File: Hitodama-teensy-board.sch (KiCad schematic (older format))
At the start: 5 parts, among them U4 Teensy3.6

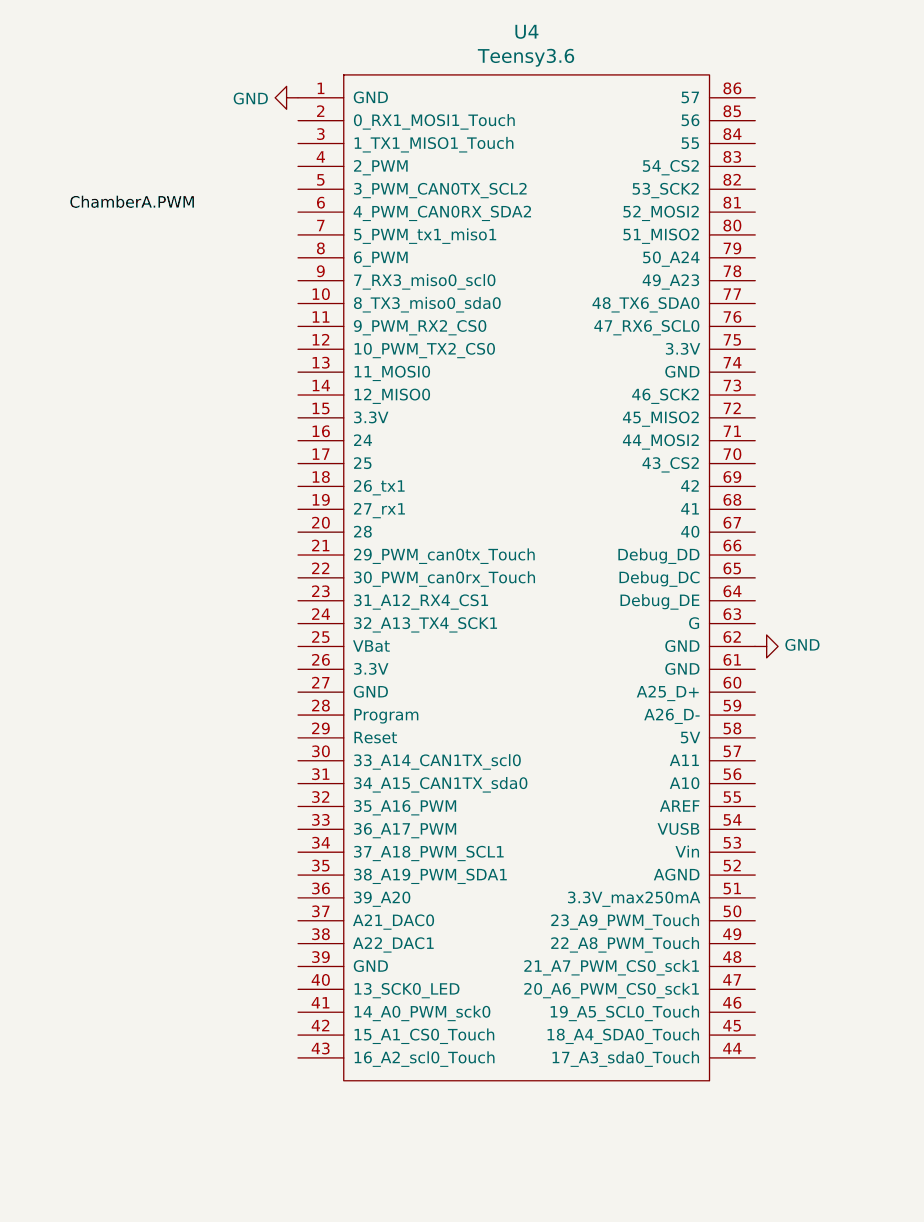
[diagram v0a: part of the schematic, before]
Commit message: Label all valve&motor controlle pins @ teensy
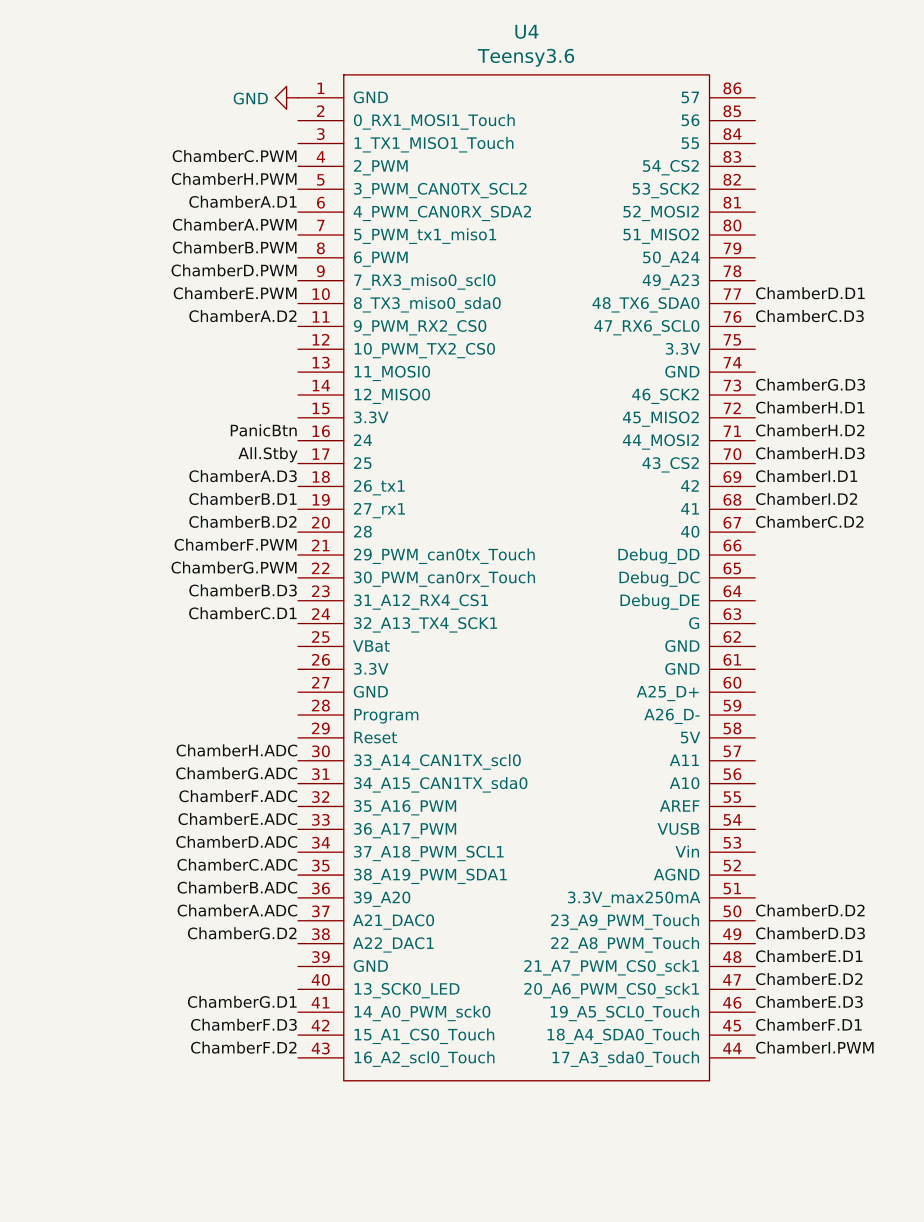
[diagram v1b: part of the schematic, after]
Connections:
- net ChamberA.PWM: now also U4.7 (5_PWM_tx1_miso1)
- net GND: no longer U4.62 (GND)
- net ChamberE.PWM: now reaches U4.10 (8_TX3_miso0_sda0)
- net ChamberA.D2: now reaches U4.11 (9_PWM_RX2_CS0)
- net PanicBtn: now reaches U4.16 (24)
- net All.Stby: now reaches U4.17 (25)
- net ChamberA.D3: now reaches U4.18 (26_tx1)
- net ChamberB.D1: now reaches U4.19 (27_rx1)
- net ChamberB.D2: now reaches U4.20 (28)
- net ChamberF.PWM: now reaches U4.21 (29_PWM_can0tx_Touch)
- net ChamberG.PWM: now reaches U4.22 (30_PWM_can0rx_Touch)
- net ChamberB.D3: now reaches U4.23 (31_A12_RX4_CS1)
- net ChamberC.D1: now reaches U4.24 (32_A13_TX4_SCK1)
- net ChamberH.ADC: now reaches U4.30 (33_A14_CAN1TX_scl0)
- net ChamberG.ADC: now reaches U4.31 (34_A15_CAN1TX_sda0)
- net ChamberF.ADC: now reaches U4.32 (35_A16_PWM)
- net ChamberE.ADC: now reaches U4.33 (36_A17_PWM)
- net ChamberD.ADC: now reaches U4.34 (37_A18_PWM_SCL1)
- net ChamberC.ADC: now reaches U4.35 (38_A19_PWM_SDA1)
- net ChamberB.ADC: now reaches U4.36 (39_A20)
- net ChamberA.ADC: now reaches U4.37 (A21_DAC0)
- net ChamberG.D2: now reaches U4.38 (A22_DAC1)
- net ChamberC.PWM: now reaches U4.4 (2_PWM)
- net ChamberG.D1: now reaches U4.41 (14_A0_PWM_sck0)
- net ChamberF.D3: now reaches U4.42 (15_A1_CS0_Touch)
- net ChamberF.D2: now reaches U4.43 (16_A2_scl0_Touch)
- net ChamberI.PWM: now reaches U4.44 (17_A3_sda0_Touch)
- net ChamberF.D1: now reaches U4.45 (18_A4_SDA0_Touch)
- net ChamberE.D3: now reaches U4.46 (19_A5_SCL0_Touch)
- net ChamberE.D2: now reaches U4.47 (20_A6_PWM_CS0_sck1)
- net ChamberE.D1: now reaches U4.48 (21_A7_PWM_CS0_sck1)
- net ChamberD.D3: now reaches U4.49 (22_A8_PWM_Touch)
- net ChamberH.PWM: now reaches U4.5 (3_PWM_CAN0TX_SCL2)
- net ChamberD.D2: now reaches U4.50 (23_A9_PWM_Touch)
- net ChamberA.D1: now reaches U4.6 (4_PWM_CAN0RX_SDA2)
- net ChamberC.D2: now reaches U4.67 (40)
- net ChamberI.D2: now reaches U4.68 (41)
- net ChamberI.D1: now reaches U4.69 (42)
- net ChamberH.D3: now reaches U4.70 (43_CS2)
- net ChamberH.D2: now reaches U4.71 (44_MOSI2)
- net ChamberH.D1: now reaches U4.72 (45_MISO2)
- net ChamberG.D3: now reaches U4.73 (46_SCK2)
- net ChamberC.D3: now reaches U4.76 (47_RX6_SCL0)
- net ChamberD.D1: now reaches U4.77 (48_TX6_SDA0)
- net ChamberB.PWM: now reaches U4.8 (6_PWM)
- net ChamberD.PWM: now reaches U4.9 (7_RX3_miso0_scl0)
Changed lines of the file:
@@
 EESchema Schematic File Version 4
+LIBS:Hitodama-teensy-board-cache
 EELAYER 26 0
 EELAYER END
@@
 	1    7150 1250
 	0    1    1    0
-$EndComp
-$Comp
-L power:GND #PWR0102
-U 1 1 5CB5BA86
-P 9150 3650
-F 0 "#PWR0102" H 9150 3400 50  0001 C CNN
-F 1 "GND" V 9155 3522 50  0000 R CNN
-F 2 "" H 9150 3650 50  0001 C CNN
-F 3 "" H 9150 3650 50  0001 C CNN
-	1    9150 3650
-	0    -1   -1   0
 $EndComp
 $Comp
@@
 	1    0    0    -1
 $EndComp
-Text Label 6150 1750 0    50   ~ 0
+Text Label 7150 1850 2    50   ~ 0
 ChamberA.PWM
+Text Label 7150 1950 2    50   ~ 0
+ChamberB.PWM
+Text Label 7150 1550 2    50   ~ 0
+ChamberC.PWM
+Text Label 7150 2050 2    50   ~ 0
+ChamberD.PWM
+Text Label 7150 2150 2    50   ~ 0
+ChamberE.PWM
+Text Label 7150 3250 2    50   ~ 0
+ChamberF.PWM
+Text Label 7150 3350 2    50   ~ 0
+ChamberG.PWM
+Text Label 7150 1650 2    50   ~ 0
+ChamberH.PWM
+Text Label 9150 5450 0    50   ~ 0
+ChamberI.PWM
+Text Label 7150 1750 2    50   ~ 0
+ChamberA.D1
+Text Label 7150 3050 2    50   ~ 0
+ChamberB.D1
+Text Label 7150 3550 2    50   ~ 0
+ChamberC.D1
+Text Label 9150 2150 0    50   ~ 0
+ChamberD.D1
+Text Label 9150 5050 0    50   ~ 0
+ChamberE.D1
+Text Label 9150 5350 0    50   ~ 0
+ChamberF.D1
+Text Label 7150 5250 2    50   ~ 0
+ChamberG.D1
+Text Label 9150 2650 0    50   ~ 0
+ChamberH.D1
+Text Label 9150 2950 0    50   ~ 0
+ChamberI.D1
+Text Label 7150 2250 2    50   ~ 0
+ChamberA.D2
+Text Label 7150 3150 2    50   ~ 0
+ChamberB.D2
+Text Label 9150 3150 0    50   ~ 0
+ChamberC.D2
+Text Label 9150 4850 0    50   ~ 0
+ChamberD.D2
+Text Label 9150 5150 0    50   ~ 0
+ChamberE.D2
+Text Label 7150 5450 2    50   ~ 0
+ChamberF.D2
+Text Label 7150 4950 2    50   ~ 0
+ChamberG.D2
+Text Label 9150 2750 0    50   ~ 0
+ChamberH.D2
+Text Label 9150 3050 0    50   ~ 0
+ChamberI.D2
+Text Label 7150 2950 2    50   ~ 0
+ChamberA.D3
+Text Label 7150 3450 2    50   ~ 0
+ChamberB.D3
+Text Label 9150 2250 0    50   ~ 0
+ChamberC.D3
+Text Label 9150 4950 0    50   ~ 0
+ChamberD.D3
+Text Label 9150 5250 0    50   ~ 0
+ChamberE.D3
+Text Label 7150 5350 2    50   ~ 0
+ChamberF.D3
+Text Label 9150 2550 0    50   ~ 0
+ChamberG.D3
+Text Label 9150 2850 0    50   ~ 0
+ChamberH.D3
+Text Label 7150 4850 2    50   ~ 0
+ChamberA.ADC
+Text Label 7150 4750 2    50   ~ 0
+ChamberB.ADC
+Text Label 7150 4650 2    50   ~ 0
+ChamberC.ADC
+Text Label 7150 4550 2    50   ~ 0
+ChamberD.ADC
+Text Label 7150 4450 2    50   ~ 0
+ChamberE.ADC
+Text Label 7150 4350 2    50   ~ 0
+ChamberF.ADC
+Text Label 7150 4250 2    50   ~ 0
+ChamberG.ADC
+Text Label 7150 4150 2    50   ~ 0
+ChamberH.ADC
+Text Label 7150 2750 2    50   ~ 0
+PanicBtn
+Text Label 7150 2850 2    50   ~ 0
+All.Stby
 $EndSCHEMATC

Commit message: Coordinate Connectors on both boards
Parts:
- added ChamberA1, ChamberB1, ChamberC1, ChamberD1, ChamberE1, ChamberF1, ChamberG1, ChamberH1, ChamberI1: ChamberBoard_Holder, chamber_board_holder:chamber_board_holder, symbol Hitodama~custom~parts:ChamberBoard_Holder
- added H5, H6: MountingHole, MountingHole:MountingHole_3.2mm_M3, symbol Mechanical:MountingHole
- added J1: Conn_01x12_Male, Connector_PinHeader_1.27mm:PinHeader_1x12_P1.27mm_Vertical, symbol Connector:Conn_01x12_Male
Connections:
- net labels added: +12V, +3.3V, A10, A11, A24, ChamberI.ADC, ChamberI.D3, D51, D52, D53, D54, D56, D57, SPI0.CS0, SPI0.MISO, SPI0.MOSI, SPI0.SCK, VCC
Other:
- moved on the sheet: H1, H2, H3, H4, U4

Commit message: schematic add SPI ports & 12 v power connector
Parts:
- removed J1: Conn_01x12_Male, Connector_PinHeader_1.27mm:PinHeader_1x12_P1.27mm_Vertical, symbol Connector:Conn_01x12_Male
- added J1: Jack-DC, Connector_BarrelJack:BarrelJack_Horizontal, symbol Connector:Jack-DC
- added SPIO_0, SPIO_1, SPIO_2, SPIO_3, SPIO_4: Conn_01x06_Female, Connector_PinHeader_2.54mm:PinHeader_1x06_P2.54mm_Vertical, symbol Connector:Conn_01x06_Female
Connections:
- net labels added: SPI0.CS1, SPI0.CS2, SPI0.CS3, SPI0.CS4
- net labels removed: D51, D52, D53, D54

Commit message: separated the teensy board into four modules, so that it fits in smaller PCB's. Improved the chamber board, and added rules so that auto-router can figure out the optimal 1 layer+jumpers route
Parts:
- removed ChamberA1, ChamberB1, ChamberC1, ChamberD1, ChamberE1, ChamberF1, ChamberG1, ChamberH1, ChamberI1: ChamberBoard_Holder, chamber_board_holder:chamber_board_holder, symbol Hitodama~custom~parts:ChamberBoard_Holder
- added J2, J3, J4: Conn_01x21_Female, Connector_PinHeader_2.54mm:PinHeader_1x21_P2.54mm_Vertical, symbol Connector:Conn_01x21_Female
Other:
- moved on the sheet: H1, H2, H3, H4, H5, H6, J1, SPIO_0, SPIO_1, SPIO_2, SPIO_3, SPIO_4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

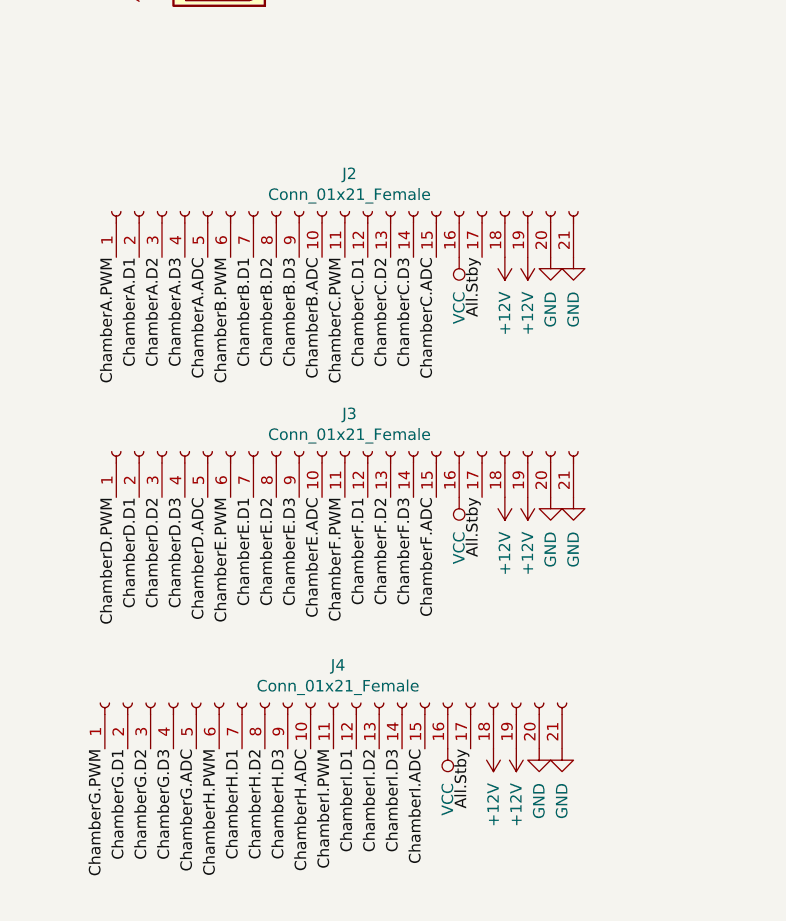
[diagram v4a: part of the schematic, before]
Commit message: teensy board change 21 pins headers into 20 pins headers.
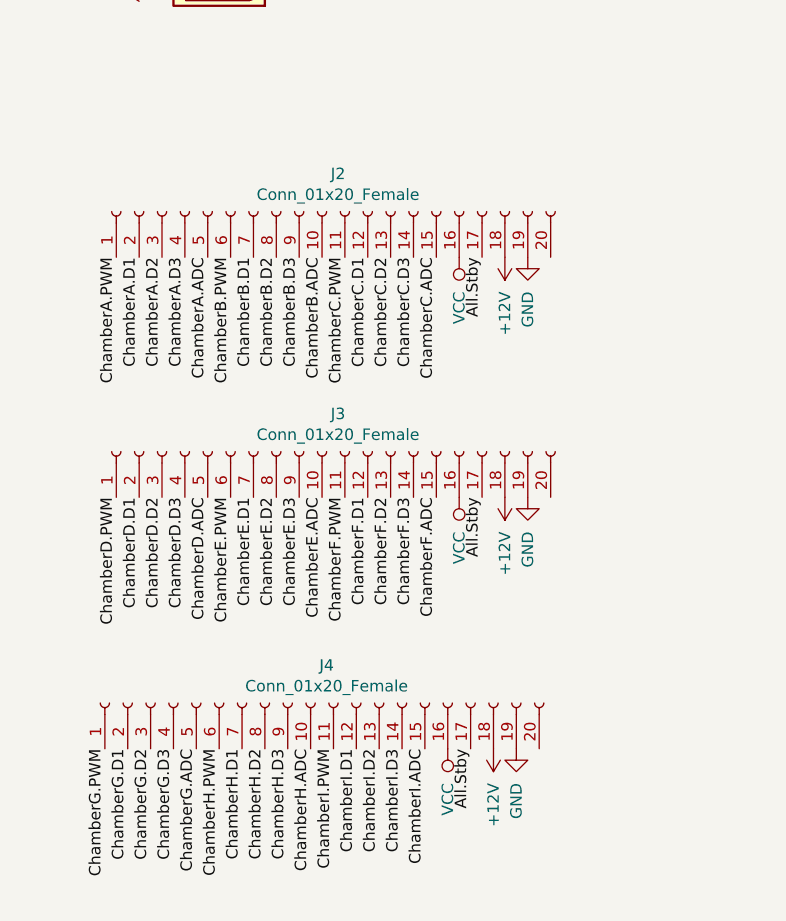
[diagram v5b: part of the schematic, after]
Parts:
- removed J2, J3, J4: Conn_01x21_Female, Connector_PinHeader_2.54mm:PinHeader_1x21_P2.54mm_Vertical, symbol Connector:Conn_01x21_Female
- added J2, J3, J4: Conn_01x20_Female, Connector_PinHeader_2.54mm:PinHeader_1x20_P2.54mm_Vertical, symbol Connector:Conn_01x20_Female
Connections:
- net +12V: now also J2.18 (Pin_18), J3.18 (Pin_18), J4.18 (Pin_18)
- net All.Stby: now also J2.17 (Pin_17), J3.17 (Pin_17), J4.17 (Pin_17)
- net ChamberA.ADC: now also J2.5 (Pin_5)
- net ChamberA.D1: now also J2.2 (Pin_2)
- net ChamberA.D2: now also J2.3 (Pin_3)
- net ChamberA.D3: now also J2.4 (Pin_4)
- net ChamberA.PWM: now also J2.1 (Pin_1)
- net ChamberB.ADC: now also J2.10 (Pin_10)
- net ChamberB.D1: now also J2.7 (Pin_7)
- net ChamberB.D2: now also J2.8 (Pin_8)
- net ChamberB.D3: now also J2.9 (Pin_9)
- net ChamberB.PWM: now also J2.6 (Pin_6)
- net ChamberC.ADC: now also J2.15 (Pin_15)
- net ChamberC.D1: now also J2.12 (Pin_12)
- net ChamberC.D2: now also J2.13 (Pin_13)
- net ChamberC.D3: now also J2.14 (Pin_14)
- net ChamberC.PWM: now also J2.11 (Pin_11)
- net ChamberD.ADC: now also J3.5 (Pin_5)
- net ChamberD.D1: now also J3.2 (Pin_2)
- net ChamberD.D2: now also J3.3 (Pin_3)
- net ChamberD.D3: now also J3.4 (Pin_4)
- net ChamberD.PWM: now also J3.1 (Pin_1)
- net ChamberE.ADC: now also J3.10 (Pin_10)
- net ChamberE.D1: now also J3.7 (Pin_7)
- net ChamberE.D2: now also J3.8 (Pin_8)
- net ChamberE.D3: now also J3.9 (Pin_9)
- net ChamberE.PWM: now also J3.6 (Pin_6)
- net ChamberF.ADC: now also J3.15 (Pin_15)
- net ChamberF.D1: now also J3.12 (Pin_12)
- net ChamberF.D2: now also J3.13 (Pin_13)
- net ChamberF.D3: now also J3.14 (Pin_14)
- net ChamberF.PWM: now also J3.11 (Pin_11)
- net ChamberG.ADC: now also J4.5 (Pin_5)
- net ChamberG.D1: now also J4.2 (Pin_2)
- net ChamberG.D2: now also J4.3 (Pin_3)
- net ChamberG.D3: now also J4.4 (Pin_4)
- net ChamberG.PWM: now also J4.1 (Pin_1)
- net ChamberH.ADC: now also J4.10 (Pin_10)
- net ChamberH.D1: now also J4.7 (Pin_7)
- net ChamberH.D2: now also J4.8 (Pin_8)
- net ChamberH.D3: now also J4.9 (Pin_9)
- net ChamberH.PWM: now also J4.6 (Pin_6)
- net ChamberI.ADC: now also J4.15 (Pin_15)
- net ChamberI.D1: now also J4.12 (Pin_12)
- net ChamberI.D2: now also J4.13 (Pin_13)
- net ChamberI.D3: now also J4.14 (Pin_14)
- net ChamberI.PWM: now also J4.11 (Pin_11)
- net GND: now also J2.19 (Pin_19), J3.19 (Pin_19), J4.19 (Pin_19)
- net VCC: now also J2.16 (Pin_16), J3.16 (Pin_16), J4.16 (Pin_16)
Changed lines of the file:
@@
 	-1   0    0    1
-$EndComp
-$Comp
-L Connector:Conn_01x21_Female J2
-U 1 1 5CC810CC
-P 2200 4550
-F 0 "J2" V 2365 4530 50  0000 C CNN
-F 1 "Conn_01x21_Female" V 2274 4530 50  0000 C CNN
-F 2 "Connector_PinHeader_2.54mm:PinHeader_1x21_P2.54mm_Vertical" H 2200 4550 50  0001 C CNN
-F 3 "~" H 2200 4550 50  0001 C CNN
-	1    2200 4550
-	0    -1   -1   0
 $EndComp
 Text Label 1200 4750 3    50   ~ 0
@@
 $EndComp
 $Comp
-L power:+12V #PWR0105
-U 1 1 5CC82883
+L power:GND #PWR0106
+U 1 1 5CC8290B
 P 3000 4750
-F 0 "#PWR0105" H 3000 4600 50  0001 C CNN
-F 1 "+12V" V 3000 4900 50  0000 L CNN
+F 0 "#PWR0106" H 3000 4500 50  0001 C CNN
+F 1 "GND" V 3000 4600 50  0000 R CNN
 F 2 "" H 3000 4750 50  0001 C CNN
 F 3 "" H 3000 4750 50  0001 C CNN
 	1    3000 4750
-	-1   0    0    1
-$EndComp
-$Comp
-L power:GND #PWR0106
-U 1 1 5CC8290B
-P 3100 4750
-F 0 "#PWR0106" H 3100 4500 50  0001 C CNN
-F 1 "GND" V 3100 4600 50  0000 R CNN
-F 2 "" H 3100 4750 50  0001 C CNN
-F 3 "" H 3100 4750 50  0001 C CNN
-	1    3100 4750
-	1    0    0    -1
-$EndComp
-$Comp
-L power:GND #PWR0107
-U 1 1 5CC829E5
-P 3200 4750
-F 0 "#PWR0107" H 3200 4500 50  0001 C CNN
-F 1 "GND" V 3200 4600 50  0000 R CNN
-F 2 "" H 3200 4750 50  0001 C CNN
-F 3 "" H 3200 4750 50  0001 C CNN
-	1    3200 4750
 	1    0    0    -1
 $EndComp
@@
 	1    2700 4750
 	-1   0    0    1
-$EndComp
-$Comp
-L Connector:Conn_01x21_Female J3
-U 1 1 5CC80D90
-P 2200 5600
-F 0 "J3" V 2365 5580 50  0000 C CNN
-F 1 "Conn_01x21_Female" V 2274 5580 50  0000 C CNN
-F 2 "Connector_PinHeader_2.54mm:PinHeader_1x21_P2.54mm_Vertical" H 2200 5600 50  0001 C CNN
-F 3 "~" H 2200 5600 50  0001 C CNN
-	1    2200 5600
-	0    -1   -1   0
 $EndComp
 Text Label 1200 5800 3    50   ~ 0
@@
 $EndComp
 $Comp
-L power:+12V #PWR0110
-U 1 1 5CC80DAD
+L power:GND #PWR0111
+U 1 1 5CC80DB3
 P 3000 5800
-F 0 "#PWR0110" H 3000 5650 50  0001 C CNN
-F 1 "+12V" V 3000 5950 50  0000 L CNN
+F 0 "#PWR0111" H 3000 5550 50  0001 C CNN
+F 1 "GND" V 3000 5650 50  0000 R CNN
 F 2 "" H 3000 5800 50  0001 C CNN
 F 3 "" H 3000 5800 50  0001 C CNN
 	1    3000 5800
-	-1   0    0    1
-$EndComp
-$Comp
-L power:GND #PWR0111
-U 1 1 5CC80DB3
-P 3100 5800
-F 0 "#PWR0111" H 3100 5550 50  0001 C CNN
-F 1 "GND" V 3100 5650 50  0000 R CNN
-F 2 "" H 3100 5800 50  0001 C CNN
-F 3 "" H 3100 5800 50  0001 C CNN
-	1    3100 5800
-	1    0    0    -1
-$EndComp
-$Comp
-L power:GND #PWR0112
-U 1 1 5CC80DB9
-P 3200 5800
-F 0 "#PWR0112" H 3200 5550 50  0001 C CNN
-F 1 "GND" V 3200 5650 50  0000 R CNN
-F 2 "" H 3200 5800 50  0001 C CNN
-F 3 "" H 3200 5800 50  0001 C CNN
-	1    3200 5800
 	1    0    0    -1
 $EndComp
@@
 	1    2700 5800
 	-1   0    0    1
-$EndComp
-$Comp
-L Connector:Conn_01x21_Female J4
-U 1 1 5CC80DF5
-P 2150 6700
-F 0 "J4" V 2315 6680 50  0000 C CNN
-F 1 "Conn_01x21_Female" V 2224 6680 50  0000 C CNN
-F 2 "Connector_PinHeader_2.54mm:PinHeader_1x21_P2.54mm_Vertical" H 2150 6700 50  0001 C CNN
-F 3 "~" H 2150 6700 50  0001 C CNN
-	1    2150 6700
-	0    -1   -1   0
 $EndComp
 Text Label 1150 6900 3    50   ~ 0
@@
 $EndComp
 $Comp
-L power:+12V #PWR0115
-U 1 1 5CC80E12
+L power:GND #PWR0116
+U 1 1 5CC80E18
 P 2950 6900
-F 0 "#PWR0115" H 2950 6750 50  0001 C CNN
-F 1 "+12V" V 2950 7050 50  0000 L CNN
+F 0 "#PWR0116" H 2950 6650 50  0001 C CNN
+F 1 "GND" V 2950 6750 50  0000 R CNN
 F 2 "" H 2950 6900 50  0001 C CNN
 F 3 "" H 2950 6900 50  0001 C CNN
 	1    2950 6900
-	-1   0    0    1
-$EndComp
-$Comp
-L power:GND #PWR0116
-U 1 1 5CC80E18
-P 3050 6900
-F 0 "#PWR0116" H 3050 6650 50  0001 C CNN
-F 1 "GND" V 3050 6750 50  0000 R CNN
-F 2 "" H 3050 6900 50  0001 C CNN
-F 3 "" H 3050 6900 50  0001 C CNN
-	1    3050 6900
-	1    0    0    -1
-$EndComp
-$Comp
-L power:GND #PWR0117
-U 1 1 5CC80E1E
-P 3150 6900
-F 0 "#PWR0117" H 3150 6650 50  0001 C CNN
-F 1 "GND" V 3150 6750 50  0000 R CNN
-F 2 "" H 3150 6900 50  0001 C CNN
-F 3 "" H 3150 6900 50  0001 C CNN
-	1    3150 6900
 	1    0    0    -1
 $EndComp
@@
 	-1   0    0    1
 $EndComp
+$Comp
+L Connector:Conn_01x20_Female J2
+U 1 1 5CCAA497
+P 2100 4550
+F 0 "J2" V 2265 4480 50  0000 C CNN
+F 1 "Conn_01x20_Female" V 2174 4480 50  0000 C CNN
+F 2 "Connector_PinHeader_2.54mm:PinHeader_1x20_P2.54mm_Vertical" H 2100 4550 50  0001 C CNN
+F 3 "~" H 2100 4550 50  0001 C CNN
+	1    2100 4550
+	0    -1   -1   0
+$EndComp
+$Comp
+L Connector:Conn_01x20_Female J3
+U 1 1 5CCAA7C7
+P 2100 5600
+F 0 "J3" V 2265 5530 50  0000 C CNN
+F 1 "Conn_01x20_Female" V 2174 5530 50  0000 C CNN
+F 2 "Connector_PinHeader_2.54mm:PinHeader_1x20_P2.54mm_Vertical" H 2100 5600 50  0001 C CNN
+F 3 "~" H 2100 5600 50  0001 C CNN
+	1    2100 5600
+	0    -1   -1   0
+$EndComp
+$Comp
+L Connector:Conn_01x20_Female J4
+U 1 1 5CCAA801
+P 2050 6700
+F 0 "J4" V 2215 6630 50  0000 C CNN
+F 1 "Conn_01x20_Female" V 2124 6630 50  0000 C CNN
+F 2 "Connector_PinHeader_2.54mm:PinHeader_1x20_P2.54mm_Vertical" H 2050 6700 50  0001 C CNN
+F 3 "~" H 2050 6700 50  0001 C CNN
+	1    2050 6700
+	0    -1   -1   0
+$EndComp
 $EndSCHEMATC
